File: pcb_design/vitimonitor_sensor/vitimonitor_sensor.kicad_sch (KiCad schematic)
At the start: 47 parts, among them J1 USB_C_Receptacle_USB2.0_14P, J2 Conn_01x10, J3 Conn_01x02, J4 Conn_01x04, J5 Pin_2x5, J6 Conn_01x04, Q2 Si2371EDS, SW1 BOOT, SW2 RESETN, U1 ESP32-C3-WROOM-02U, U2 USBLC6-2SC6, U3 LM1117DT-3.3, U5 BQ24075RGT

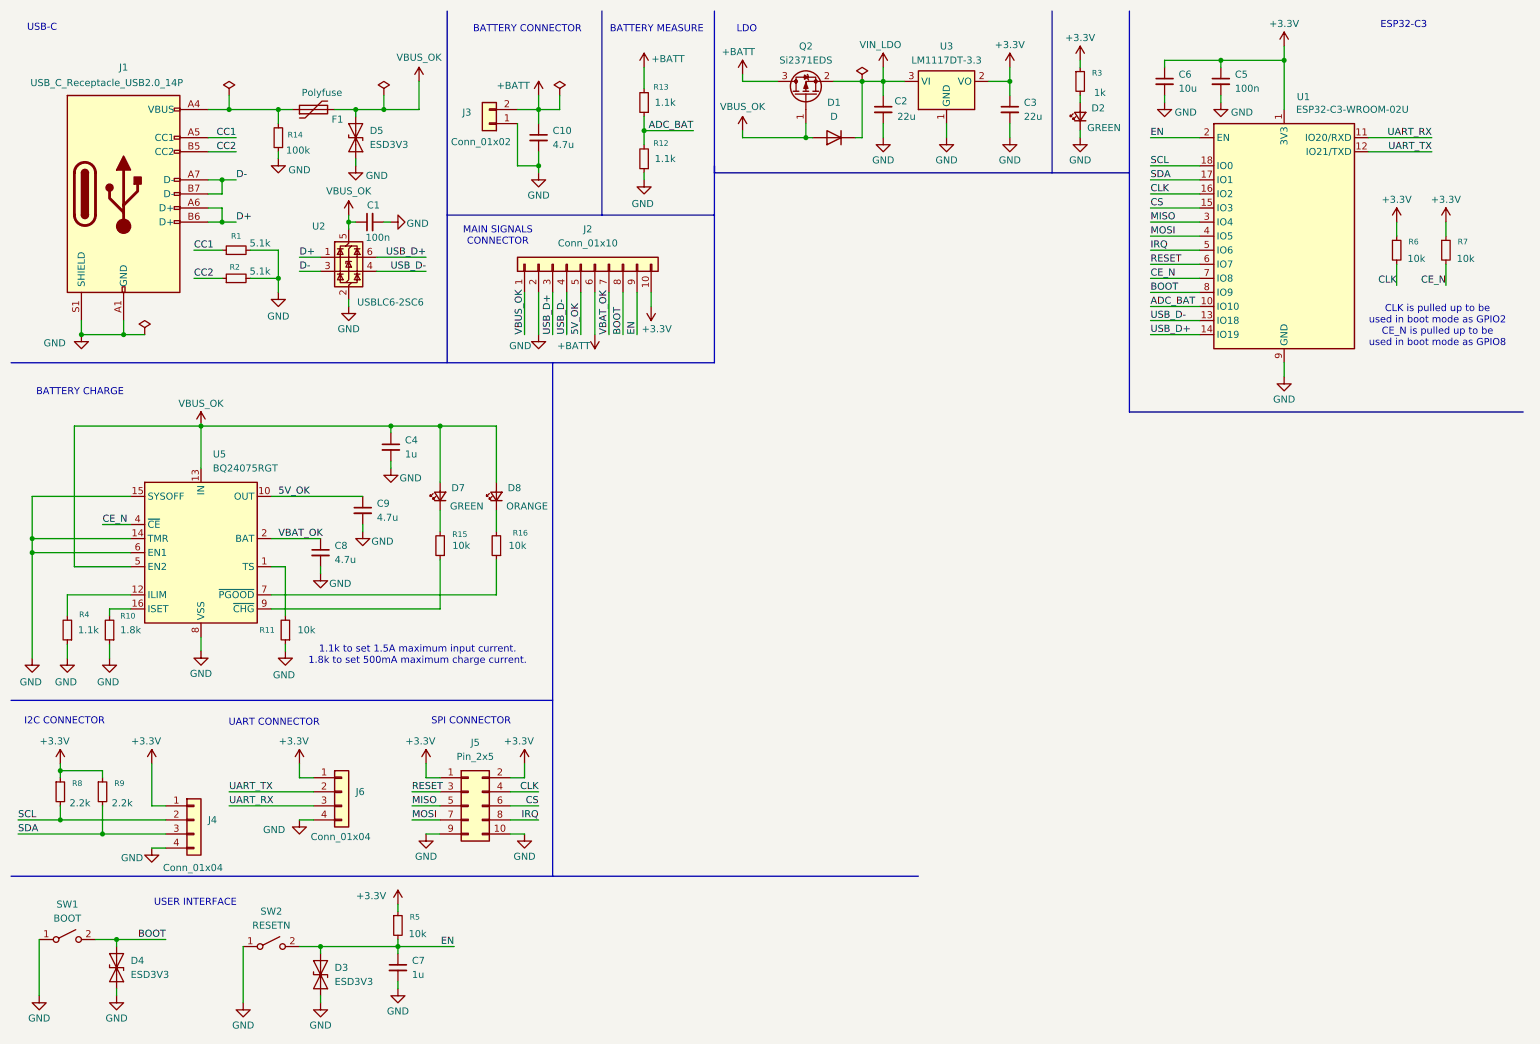
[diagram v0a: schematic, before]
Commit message: Hierarchical schematic almost done
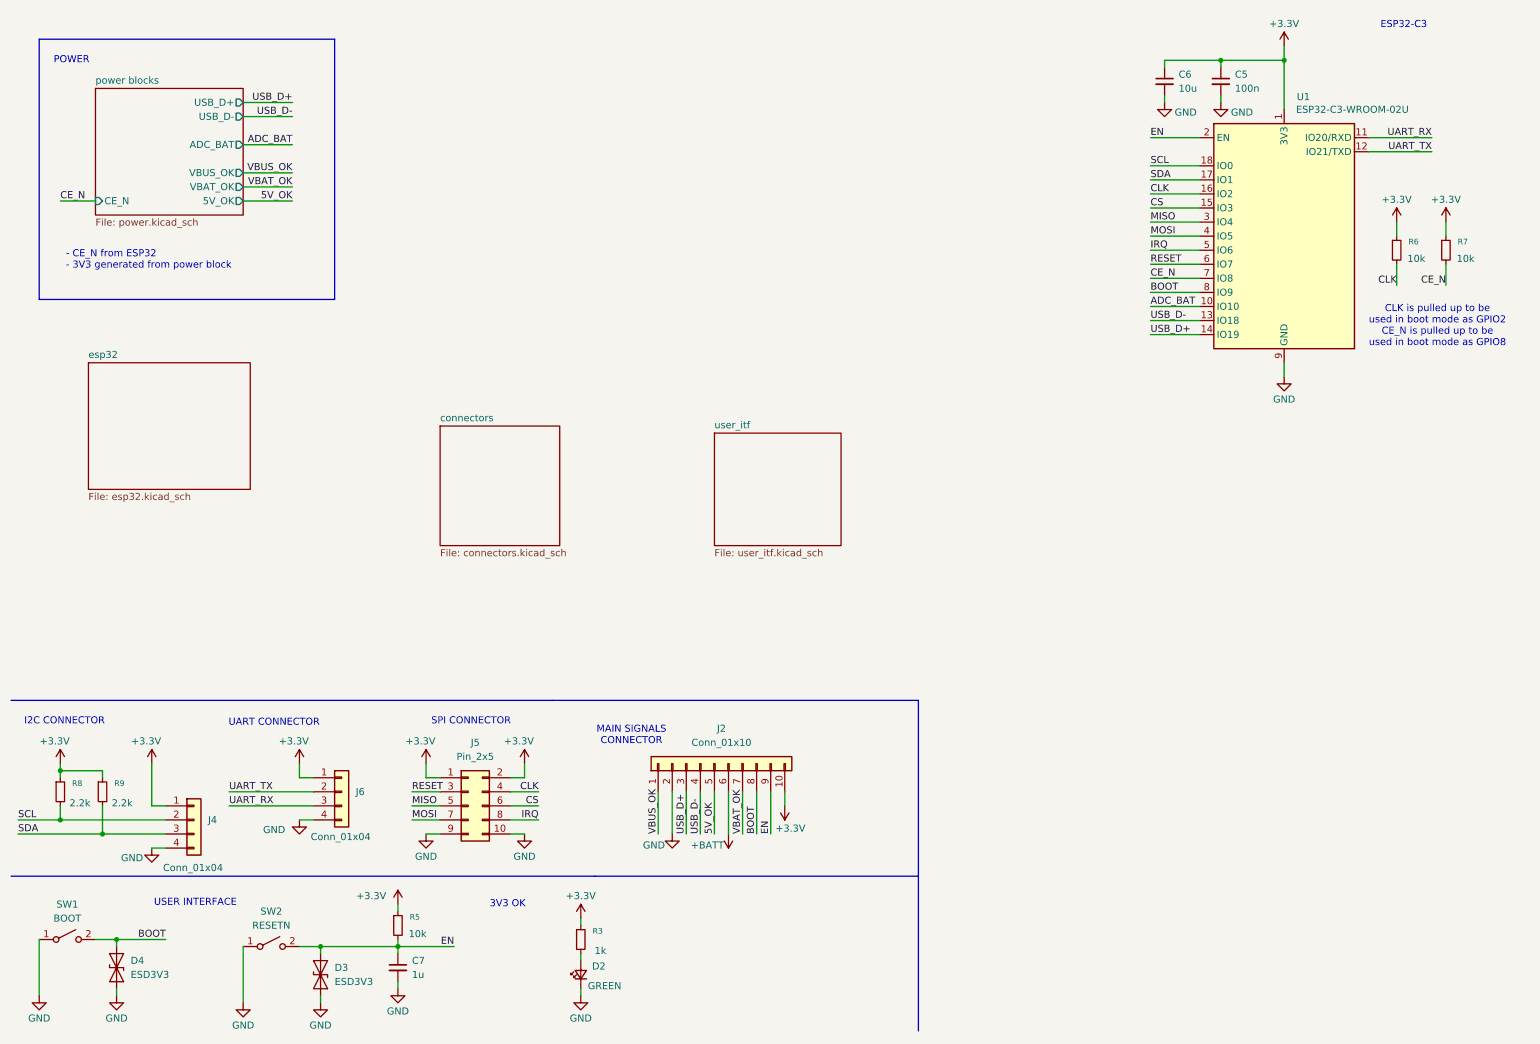
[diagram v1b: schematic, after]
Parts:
- removed C1: 100n, symbol Device:C_Small
- removed C10, C8, C9: 4.7u, symbol Device:C_Small
- removed C2, C3: 22u, symbol Device:C_Small
- removed C4: 1u, symbol Device:C_Small
- removed D1: D, symbol Device:D
- removed D5: ESD3V3, Diode_SMD:D_SOD-923, symbol Diode:ESD9B3.3ST5G
- removed D7: GREEN, symbol Device:LED_Small
- removed D8: ORANGE, symbol Device:LED_Small
- removed F1: Polyfuse, symbol Device:Polyfuse
- removed J1: USB_C_Receptacle_USB2.0_14P, symbol Connector:USB_C_Receptacle_USB2.0_14P
- removed J3: Conn_01x02, symbol Connector_Generic:Conn_01x02
- removed Q2: Si2371EDS, Package_TO_SOT_SMD:SOT-23, symbol Transistor_FET:Si2371EDS
- removed R1, R2: 5.1k, symbol Device:R_Small
- removed R10: 1.8k, symbol Device:R_Small
- removed R11, R15, R16: 10k, symbol Device:R_Small
- removed R12, R13, R4: 1.1k, symbol Device:R_Small
- removed R14: 100k, symbol Device:R_Small
- removed U2: USBLC6-2SC6, Package_TO_SOT_SMD:SOT-23-6, symbol Power_Protection:USBLC6-2SC6
- removed U3: LM1117DT-3.3, Package_TO_SOT_SMD:TO-252-3_TabPin2, symbol Regulator_Linear:LM1117DT-3.3
- removed U5: BQ24075RGT, Package_DFN_QFN:VQFN-16-1EP_3x3mm_P0.5mm_EP1.6x1.6mm, symbol Battery_Management:BQ24075RGT
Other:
- added sheet connectors (connectors.kicad_sch)
- added sheet esp32 (esp32.kicad_sch)
- added sheet power blocks (power.kicad_sch)
- added sheet user_itf (user_itf.kicad_sch)
- note added: "- CE_N from ESP32 - 3V3 generated from power block"
- note added: "3V3 OK"
- note added: "POWER"
- note removed: "1.1k to set 1.5A maximum input current. 1.8k to set 500mA maximum charge current."
- note removed: "BATTERY CHARGE"
- note removed: "BATTERY CONNECTOR"
- note removed: "BATTERY MEASURE"
- note removed: "LDO"
- note removed: "USB-C"
- moved on the sheet: D2, J2, R3

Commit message: Schematic update, hierarchical approach done, missing SX1261
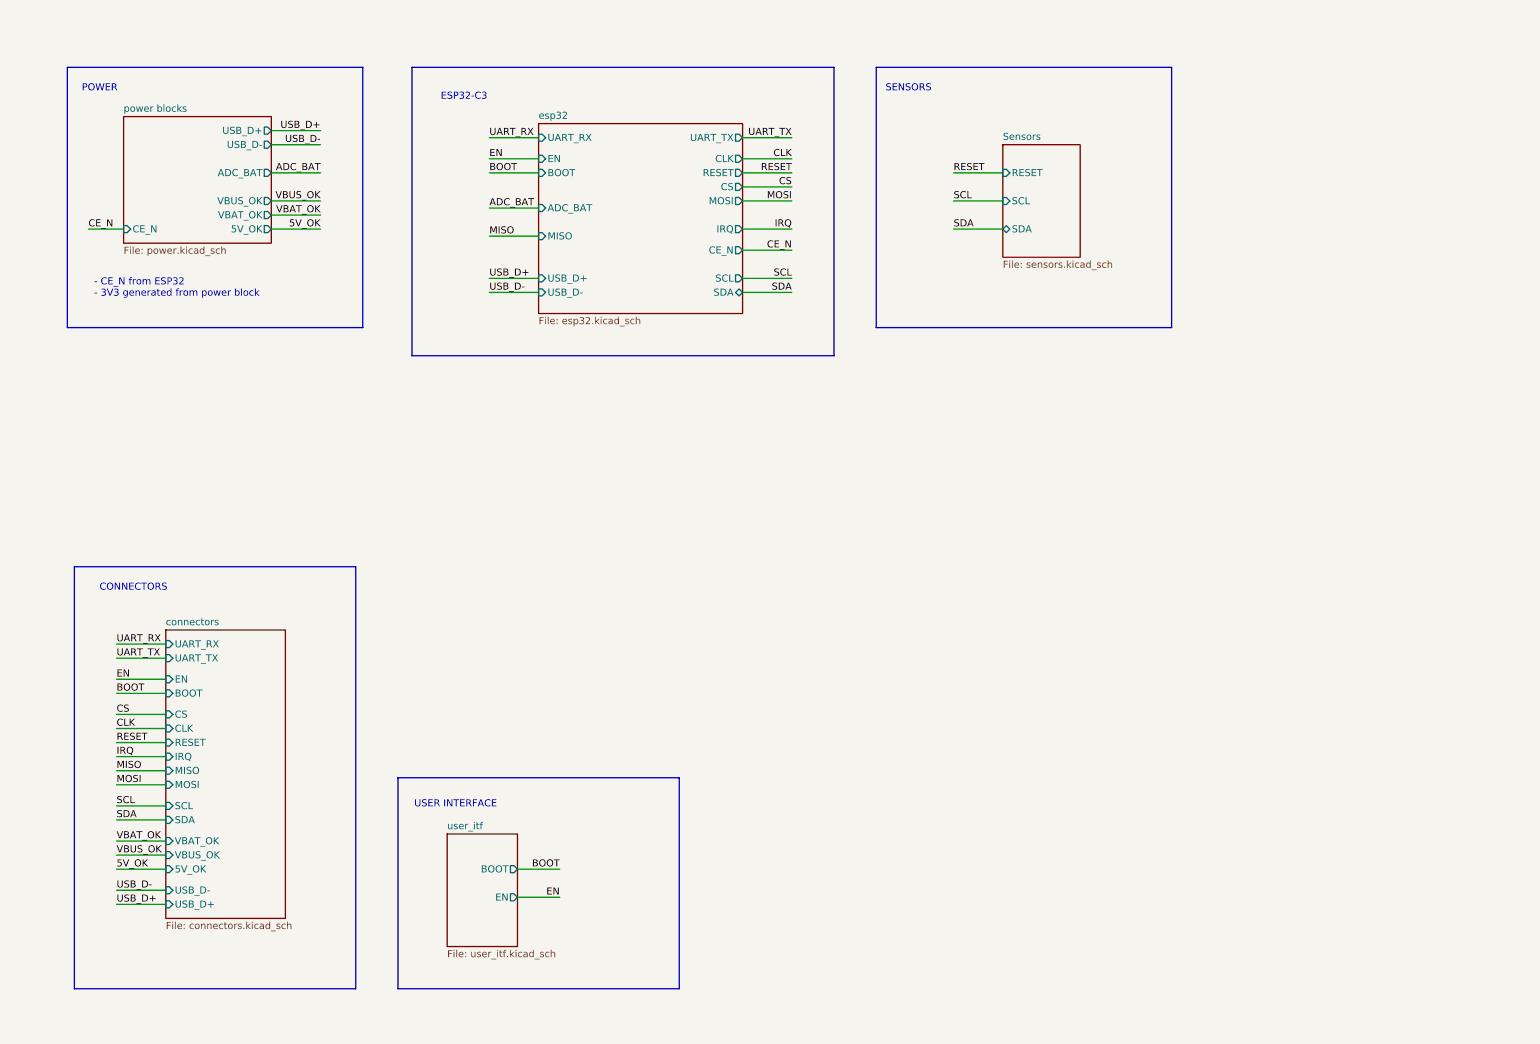
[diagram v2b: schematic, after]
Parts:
- removed C5: 100n, symbol Device:C_Small
- removed C6: 10u, symbol Device:C_Small
- removed C7: 1u, symbol Device:C_Small
- removed D2: GREEN, symbol Device:LED_Small
- removed D3, D4: ESD3V3, Diode_SMD:D_SOD-923, symbol Diode:ESD9B3.3ST5G
- removed J2: Conn_01x10, symbol Connector_Generic:Conn_01x10
- removed J4, J6: Conn_01x04, symbol Connector_Generic:Conn_01x04
- removed J5: Pin_2x5, symbol Connector_Generic:Conn_02x05_Odd_Even
- removed R3: 1k, symbol Device:R_Small
- removed R5, R6, R7: 10k, symbol Device:R_Small
- removed R8, R9: 2.2k, symbol Device:R_Small
- removed SW1: BOOT, symbol Switch:SW_SPST
- removed SW2: RESETN, symbol Switch:SW_SPST
- removed U1: ESP32-C3-WROOM-02U, RF_Module:ESP32-C3-WROOM-02U, symbol RF_Module:ESP32-C3-WROOM-02U
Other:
- added sheet Sensors (sensors.kicad_sch)
- sheet connectors ports: added 5V_OK, BOOT, CLK, CS, EN, IRQ, MISO, MOSI, RESET, SCL, SDA, UART_RX, UART_TX, USB_D+, USB_D-, VBAT_OK, VBUS_OK; removed none
- sheet esp32 ports: added ADC_BAT, BOOT, CE_N, CLK, CS, EN, IRQ, MISO, MOSI, RESET, SCL, SDA, UART_RX, UART_TX, USB_D+, USB_D-; removed none
- sheet user_itf ports: added BOOT, EN; removed none
- note added: "CONNECTORS"
- note added: "SENSORS"
- note removed: "3V3 OK"
- note removed: "CLK is pulled up to be used in boot mode as GPIO2 CE_N is pulled up to be used in boot mode as GPIO8"
- note removed: "I2C CONNECTOR"
- note removed: "MAIN SIGNALS CONNECTOR"
- note removed: "SPI CONNECTOR"
- note removed: "UART CONNECTOR"

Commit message: Schematic update
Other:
- added sheet radio (radio.kicad_sch)
- note added: "RADIO SX1261"

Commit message: Changes due to a first review
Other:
- sheet power blocks ports: added none; removed USB_D+, USB_D-
